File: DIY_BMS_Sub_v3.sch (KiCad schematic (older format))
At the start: 50 parts, among them J1 Conn_01x11, J2 Conn_02x04_Top_Bottom, J3 Conn_02x03_Top_Bottom, J4 Conn_02x03_Top_Bottom, SW1 SW_DIP_x04, U1 BQ76PL536A

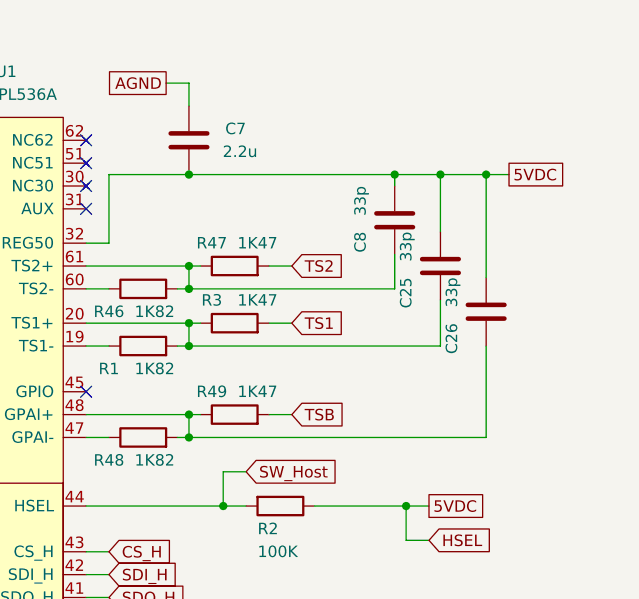
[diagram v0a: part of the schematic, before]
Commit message: Add files via upload
Added and routed board NTC. Added connector and board info silkscreen. Made keep-out zones for AGND to remove planes under components.
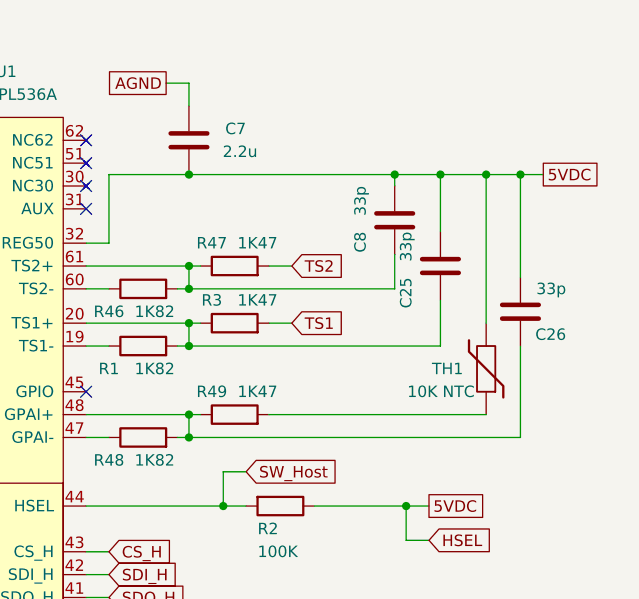
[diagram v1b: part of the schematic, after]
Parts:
- added TH1: 10K NTC, Resistor_SMD:R_0603_1608Metric_Pad0.98x0.95mm_HandSolder, symbol Device:Thermistor
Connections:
- net 5VDC: now also TH1.2
- net TSB: no longer names the net of R49.2
- net TSB: now also TH1.1
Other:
- moved on the sheet: C26
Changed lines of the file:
@@
 Wire Wire Line
 	10350 5350 10700 5350
-Text GLabel 12100 5350 2    50   UnSpc ~ 0
+Text GLabel 12250 5350 2    50   UnSpc ~ 0
 5VDC
 Connection ~ 10700 5350
@@
 Wire Wire Line
 	10700 5350 11600 5350
-Connection ~ 12000 5350
-Wire Wire Line
-	12000 5350 12100 5350
+Wire Wire Line
+	12150 5350 12250 5350
 Wire Wire Line
 	11600 5350 11600 5400
@@
 	10700 6400 10250 6400
 Connection ~ 10700 6400
-Text GLabel 11150 6400 2    50   Input ~ 0
-TSB
-Wire Wire Line
-	11150 6400 11050 6400
 Wire Wire Line
 	10350 6500 10250 6500
@@
 L Device:C C26
 U 1 1 612E89FE
-P 12000 5950
-F 0 "C26" V 12150 6000 50  0000 L CNN
-F 1 "33p" V 12150 5800 50  0000 L CNN
-F 2 "Capacitor_SMD:C_0603_1608Metric_Pad1.05x0.95mm_HandSolder" H 12038 5800 50  0001 C CNN
-F 3 "file:///C:/Users/HenkHenk/Downloads/KEM_C1007_X8R_ULTRA_150C_SMD-1102703.pdf" H 12000 5950 50  0001 C CNN
-F 4 "C1663" H 12000 5950 50  0001 C CNN "LCSC"
-	1    12000 5950
+P 12150 5950
+F 0 "C26" H 11950 6050 50  0000 L CNN
+F 1 "33p" H 11950 5850 50  0000 L CNN
+F 2 "Capacitor_SMD:C_0603_1608Metric_Pad1.05x0.95mm_HandSolder" H 12188 5800 50  0001 C CNN
+F 3 "file:///C:/Users/HenkHenk/Downloads/KEM_C1007_X8R_ULTRA_150C_SMD-1102703.pdf" H 12150 5950 50  0001 C CNN
+F 4 "C1663" H 12150 5950 50  0001 C CNN "LCSC"
+	1    12150 5950
 	-1   0    0    1
 $EndComp
@@
 Connection ~ 10700 6100
 Connection ~ 11650 6800
-Wire Wire Line
-	12000 6100 12000 6500
-Wire Wire Line
-	12000 6500 10700 6500
 Connection ~ 10700 6500
 Wire Wire Line
-	12000 5350 12000 5800
+	12150 5350 12150 5800
 Wire Wire Line
 	11800 5600 11800 5350
 Connection ~ 11800 5350
-Wire Wire Line
-	11800 5350 12000 5350
 NoConn ~ 3650 2000
 NoConn ~ 3650 2100
+$Comp
+L Device:Thermistor TH1
+U 1 1 613A86B3
+P 12000 6200
+F 0 "TH1" H 12100 6200 50  0000 L CNN
+F 1 "10K NTC" H 12050 6300 50  0000 L CNN
+F 2 "Resistor_SMD:R_0603_1608Metric_Pad0.98x0.95mm_HandSolder" H 12000 6200 50  0001 C CNN
+F 3 "https://eu.mouser.com/ProductDetail/Panasonic/ERT-J1VG103FA?qs=Tap6ps20mlMpYFuAQ7bHkg%3D%3D" H 12000 6200 50  0001 C CNN
+F 4 "ERT-J1VG103FA" H 12000 6200 50  0001 C CNN "DPN"
+	1    12000 6200
+	-1   0    0    1
+$EndComp
+Connection ~ 12150 5350
+Wire Wire Line
+	12150 6100 12150 6500
+Wire Wire Line
+	11800 5350 12000 5350
+Wire Wire Line
+	10700 6500 12150 6500
+Wire Wire Line
+	11050 6400 12000 6400
+Wire Wire Line
+	12000 6000 12000 5350
+Connection ~ 12000 5350
+Wire Wire Line
+	12000 5350 12150 5350
 $EndSCHEMATC

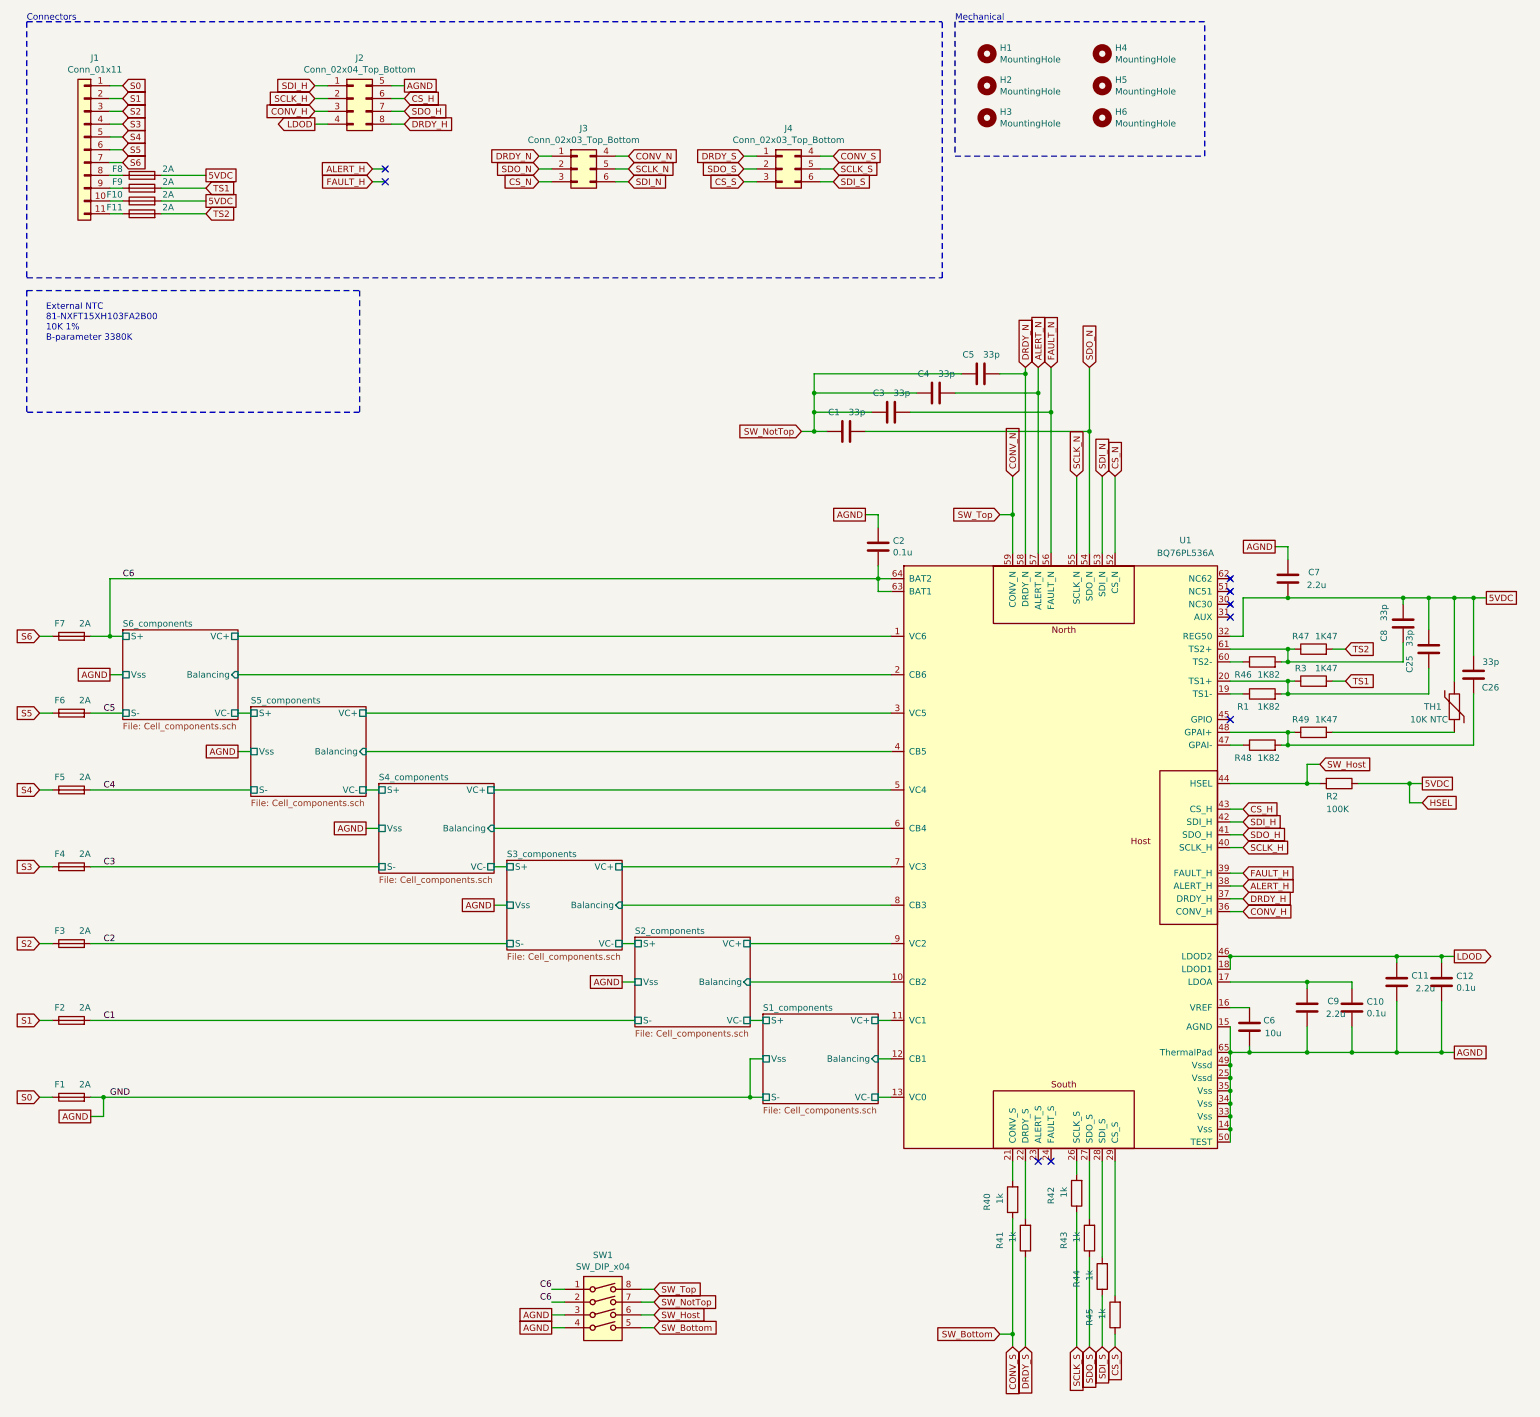
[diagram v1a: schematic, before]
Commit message: Add files via upload
Placed additional via's to BQ76-IC and removed soldermask beneath (to allow for soldering of thermal pad without hot air). Generated GERBER-, BOM- (for SMD parts) and POS-file.
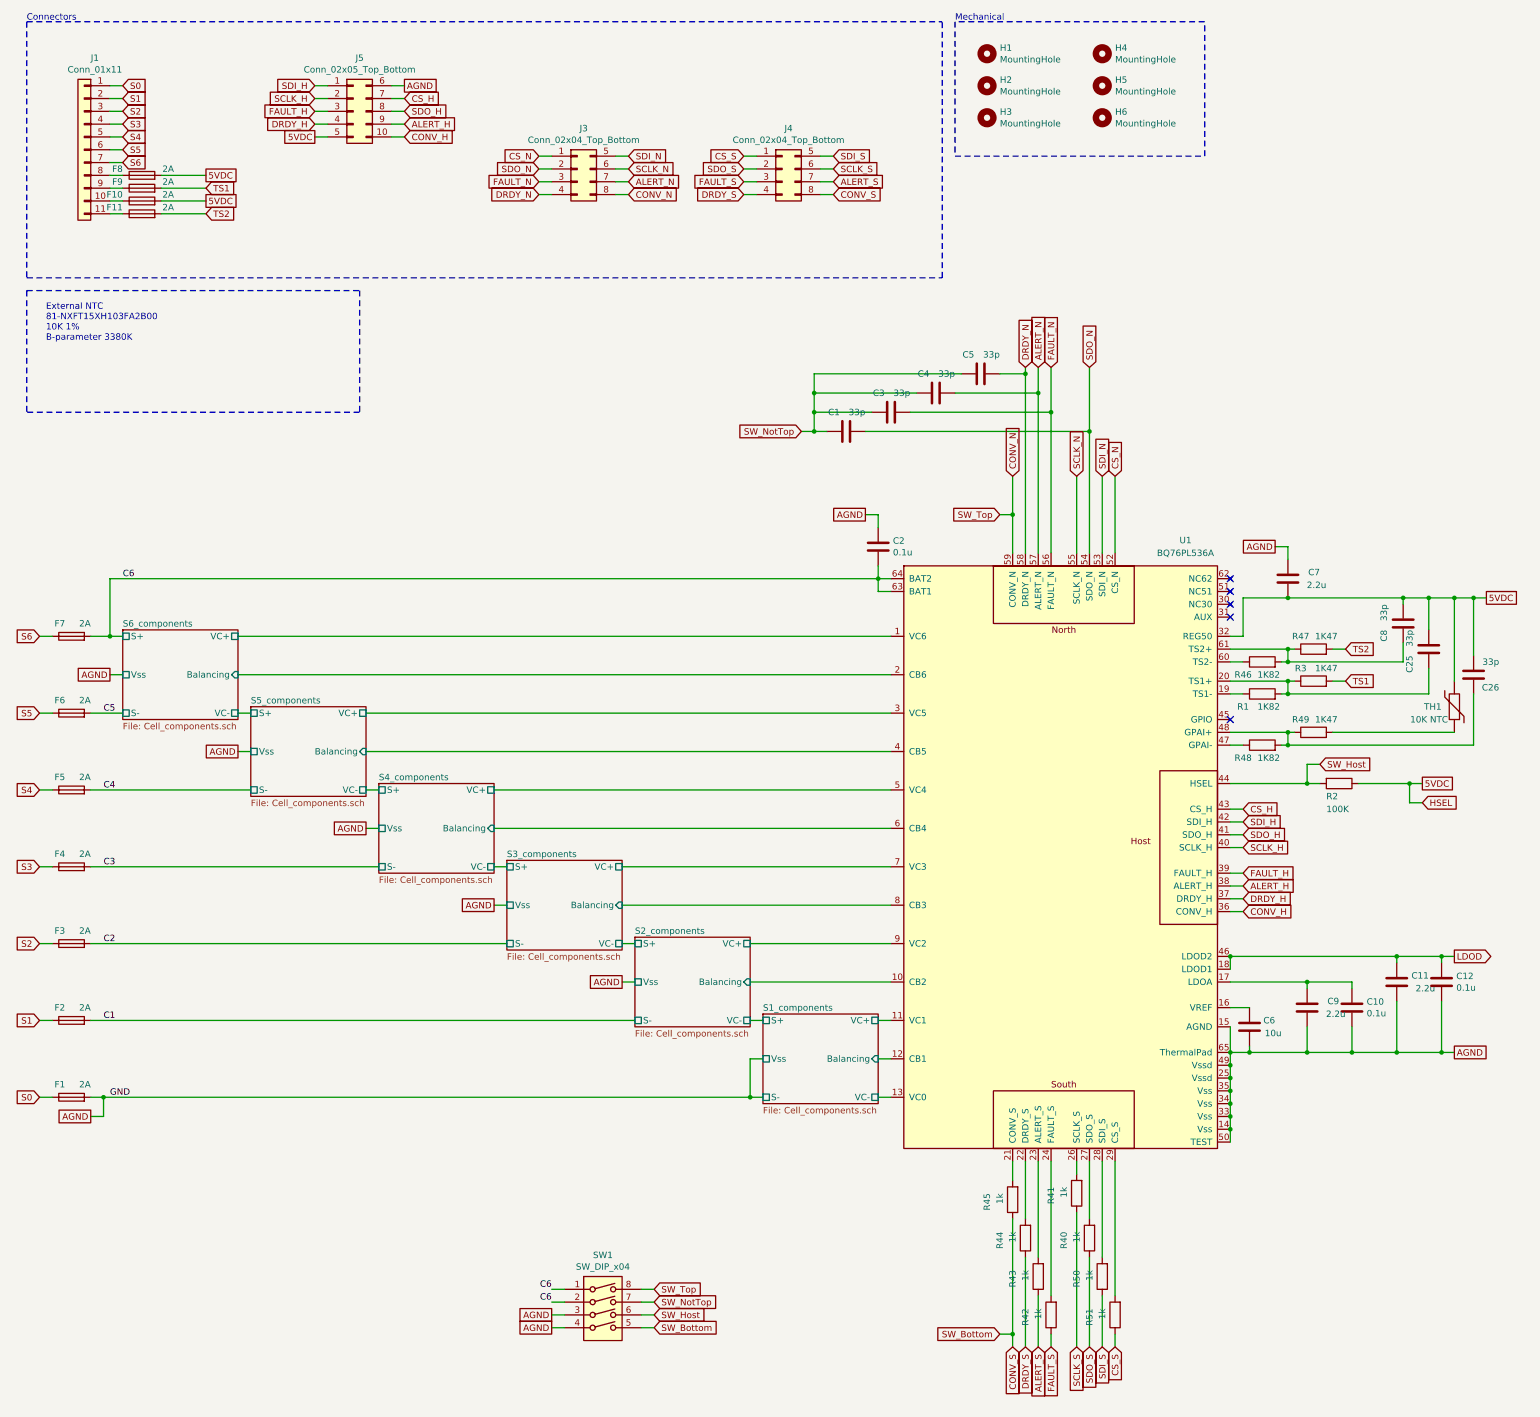
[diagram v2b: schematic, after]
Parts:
- removed J2: Conn_02x04_Top_Bottom, Connector_Molex:Molex_Micro-Fit_3.0_43045-0821_2x04-1MP_P3.00mm_Horizontal, symbol Connector_Generic:Conn_02x04_Top_Bottom
- removed J3, J4: Conn_02x03_Top_Bottom, Connector_Molex:Molex_Micro-Fit_3.0_43045-0621_2x03-1MP_P3.00mm_Horizontal, symbol Connector_Generic:Conn_02x03_Top_Bottom
- added J3, J4: Conn_02x04_Top_Bottom, Connector_Molex:Molex_Micro-Fit_3.0_43045-0800_2x04_P3.00mm_Horizontal, symbol Connector_Generic:Conn_02x04_Top_Bottom
- added J5: Conn_02x05_Top_Bottom, Connector_Molex:Molex_Micro-Fit_3.0_43045-1000_2x05_P3.00mm_Horizontal, symbol Connector_Generic:Conn_02x05_Top_Bottom
- added R50, R51: 1k, Resistor_SMD:R_0603_1608Metric_Pad1.05x0.95mm_HandSolder, symbol Device:R
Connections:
- net 5VDC: now also J5.5 (Pin_5)
- net AGND: now also J5.6 (Pin_6)
- net ALERT_H: now also J5.9 (Pin_9)
- net ALERT_N: now also J3.7 (Pin_7)
- net CONV_H: now also J5.10 (Pin_10)
- net CONV_N: now also J3.8 (Pin_8)
- net CONV_S: now also R45.1, J4.8 (Pin_8); no longer R40.1
- net CS_H: now also J5.7 (Pin_7)
- net CS_N: now also J3.1 (Pin_1)
- net CS_S: now also J4.1 (Pin_1), R51.1; no longer R45.1
- net DRDY_H: now also J5.4 (Pin_4)
- net DRDY_N: now also J3.4 (Pin_4)
- net DRDY_S: now also R44.1, J4.4 (Pin_4); no longer R41.1
- net FAULT_H: now also J5.3 (Pin_3)
- net FAULT_N: now also J3.3 (Pin_3)
- net SCLK_H: now also J5.2 (Pin_2)
- net SCLK_N: now also J3.6 (Pin_6)
- net SCLK_S: now also R41.1, J4.6 (Pin_6); no longer R42.1
- net SDI_H: now also J5.1 (Pin_1)
- net SDI_N: now also J3.5 (Pin_5)
- net SDI_S: now also J4.5 (Pin_5), R50.1; no longer R44.1
- net SDO_H: now also J5.8 (Pin_8)
- net SDO_N: now also J3.2 (Pin_2)
- net SDO_S: now also R40.1, J4.2 (Pin_2); no longer R43.1
- net at U1.21 (CONV_S): now also R45.2; no longer R40.2
- net at U1.22 (DRDY_S): now also R44.2; no longer R41.2
- net at U1.23 (ALERT_S): now also R43.2
- net at U1.24 (FAULT_S): now also R42.2
- net at U1.26 (SCLK_S): now also R41.2; no longer R42.2
- net at U1.27 (SDO_S): now also R40.2; no longer R43.2
- net at U1.28 (SDI_S): now also R50.2; no longer R44.2
- net at U1.29 (CS_S): now also R51.2; no longer R45.2
- new net ALERT_S: J4.7 (Pin_7), R43.1
- new net FAULT_S: J4.3 (Pin_3), R42.1
- no-connect marks 9 -> 5
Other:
- moved on the sheet: R40, R41, R42, R43, R44, R45
